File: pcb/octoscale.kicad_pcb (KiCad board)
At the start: 2 copper layers, 60 x 96.5 mm, 115 parts, among them J1 USB_C_Receptacle_USB2.0 TYPE-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, J2 Conn_01x04_Male, J3 Molex picoblade vertical C122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, J4 JST-SH, stemma, J5 JST-SH, J6 JST-SH, J7 Conn_01x04_Male, Q1 AO3415_C181094, Q2 MMBT44032T, Q3 S8050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

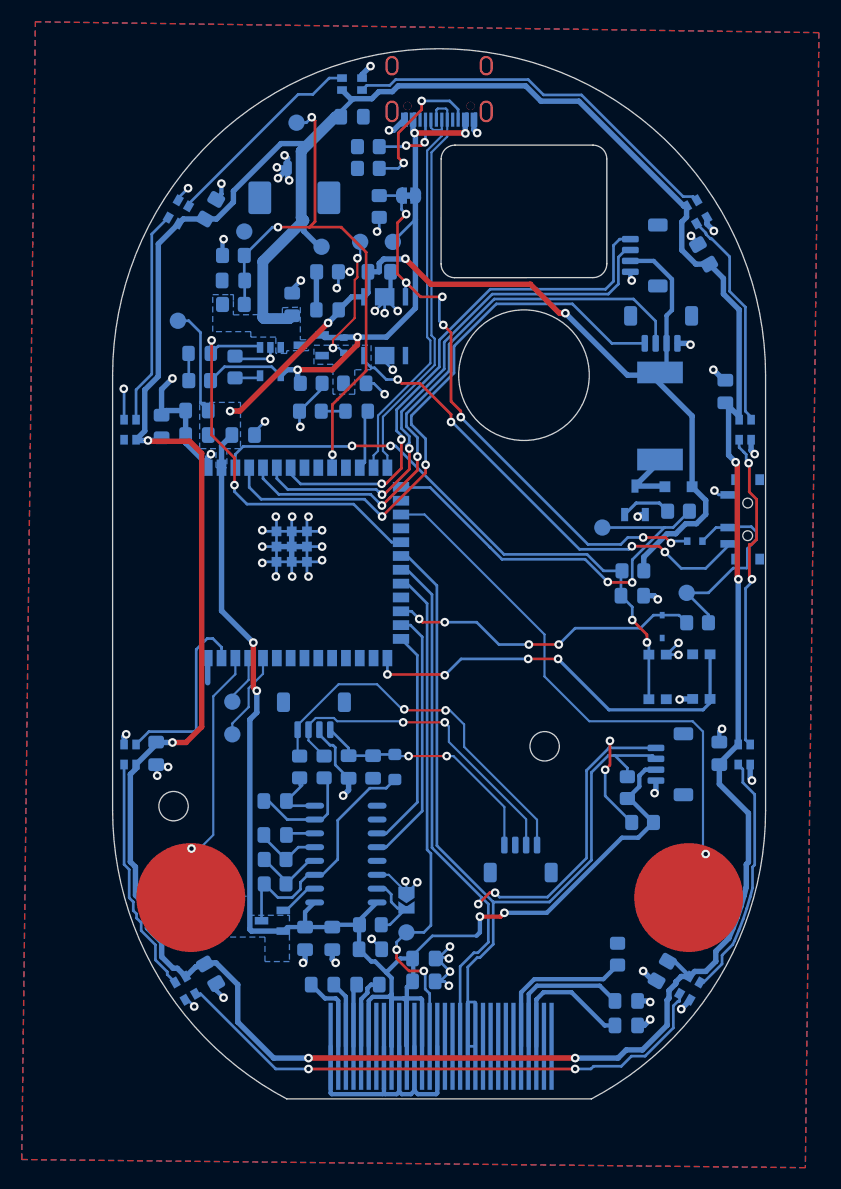
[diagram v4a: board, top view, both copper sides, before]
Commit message: Fix neopixel footprint
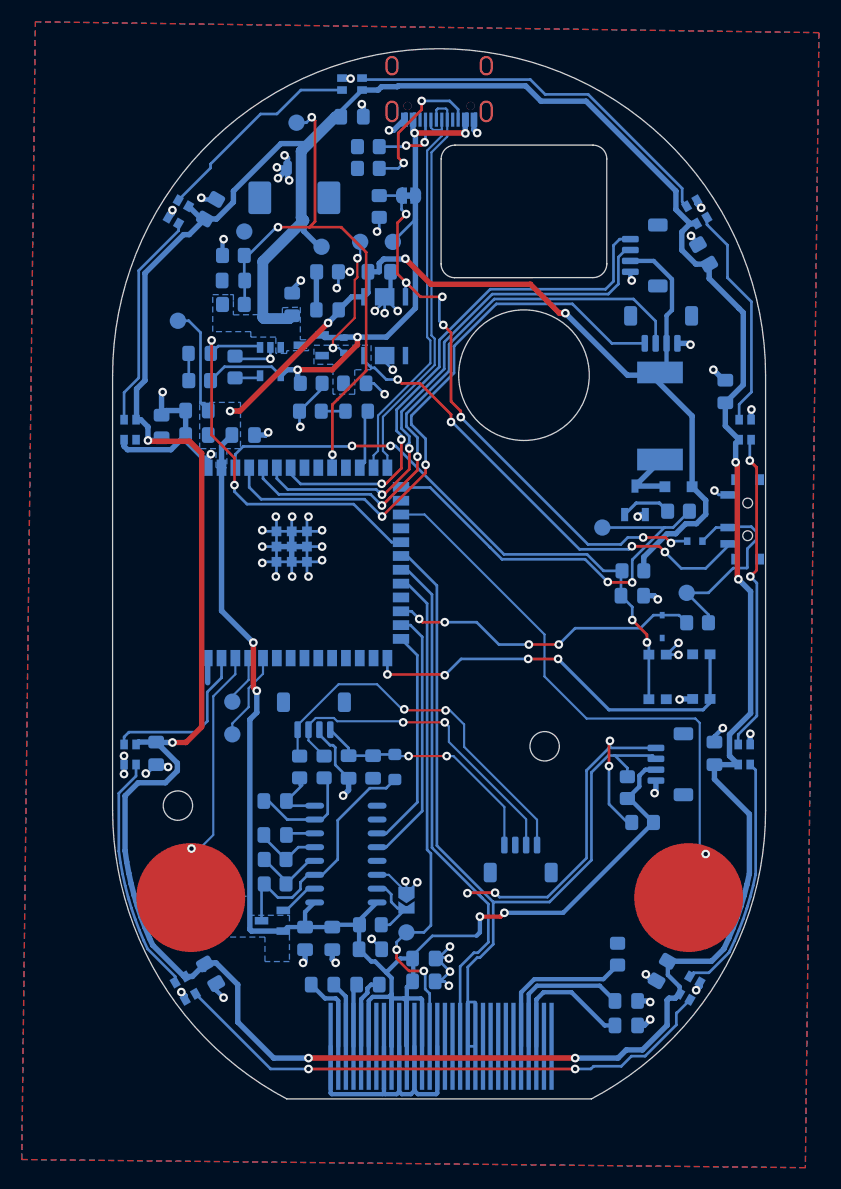
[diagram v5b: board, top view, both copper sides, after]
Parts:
- moved C27 0.45 mm to (195.3, 109.8)
- moved H2 0.40 mm to (146.0, 114.5)
- turned D1 to 120 degrees
- turned D10 to 60 degrees
- turned D11 to 90 degrees
- turned D12 to 90 degrees
- turned D3 to -120 degrees
- turned D6 to -90 degrees
- turned D7 to -90 degrees
- turned D8 to -60 degrees
- turned D9 to 0 degrees
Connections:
- D1 pad 2: GND -> +BATT
- D1 pad 4: +BATT -> GND
- D10 pad 1: +BATT -> Net-(D10-Pad1)
- D10 pad 2: Net-(D10-Pad2) -> +BATT
- D10 pad 3: GND -> Net-(D10-Pad3)
- D10 pad 4: Net-(D10-Pad4) -> GND
- D11 pad 1: +BATT -> Net-(D10-Pad3)
- D11 pad 2: unconnected-(D11-Pad2) -> +BATT
- D11 pad 3: GND -> unconnected-(D11-Pad3)
- D11 pad 4: Net-(D10-Pad2) -> GND
- D12 pad 1: +BATT -> NEOPIXELS
- D12 pad 2: Net-(D1-Pad3) -> +BATT
- D12 pad 3: GND -> Net-(D1-Pad1)
- D12 pad 4: NEOPIXELS -> GND
- D3 pad 1: +BATT -> Net-(D1-Pad3)
- D3 pad 2: Net-(D3-Pad2) -> +BATT
- D3 pad 3: GND -> Net-(D3-Pad3)
- D3 pad 4: Net-(D1-Pad1) -> GND
- D6 pad 1: +BATT -> Net-(D3-Pad3)
- D6 pad 2: Net-(D6-Pad2) -> +BATT
- D6 pad 3: GND -> Net-(D6-Pad3)
- D6 pad 4: Net-(D3-Pad2) -> GND
- D7 pad 1: +BATT -> Net-(D6-Pad3)
- D7 pad 2: Net-(D7-Pad2) -> +BATT
- D7 pad 3: GND -> Net-(D7-Pad3)
- D7 pad 4: Net-(D6-Pad2) -> GND
- D8 pad 1: +BATT -> Net-(D7-Pad3)
- D8 pad 2: Net-(D8-Pad2) -> +BATT
- D8 pad 3: GND -> Net-(D8-Pad3)
- D8 pad 4: Net-(D7-Pad2) -> GND
- D9 pad 1: +BATT -> Net-(D8-Pad3)
- D9 pad 2: Net-(D10-Pad4) -> +BATT
- D9 pad 3: GND -> Net-(D10-Pad1)
- D9 pad 4: Net-(D8-Pad2) -> GND
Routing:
- net Net-(D8-Pad2): track 35.8 -> 0.00 mm
- net Net-(D8-Pad3): track 0.00 -> 35.4 mm
- net Net-(D1-Pad1): track 51.8 -> 22.2 mm, vias 2 -> 0
- net Net-(D1-Pad3): track 22.0 -> 51.6 mm, vias 0 -> 2
- net Net-(D6-Pad2): track 29.6 -> 0.00 mm, vias 2 -> 0
- net Net-(D6-Pad3): track 0.00 -> 29.5 mm, vias 0 -> 2
- net Net-(D3-Pad2): track 22.5 -> 0.00 mm
- net Net-(D3-Pad3): track 0.00 -> 22.4 mm
- net Net-(D7-Pad3): track 0.00 -> 20.7 mm
- net Net-(D7-Pad2): track 20.2 -> 0.00 mm
- net Net-(D10-Pad3): track 0.00 -> 20.1 mm
- net Net-(D10-Pad2): track 19.8 -> 0.00 mm
- net Net-(D10-Pad1): track 0.00 -> 19.5 mm
- net Net-(D10-Pad4): track 19.1 -> 0.00 mm
- net +BATT: track 308.7 -> 316.1 mm
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
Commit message: Slight tweaks
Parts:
- moved TP11 0.75 mm to (151.8, 105.0)
- moved TP7 0.75 mm to (151.8, 108.0)
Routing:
- net LDO_EN: track 54.3 -> 53.2 mm, vias 7 -> 5
- net TOUCH_1: track 19.6 -> 18.9 mm
- net +3V3: track 247.8 -> 248.5 mm
